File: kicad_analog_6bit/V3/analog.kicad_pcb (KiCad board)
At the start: 2 copper layers, 50 x 23.2 mm, 35 parts, among them P1 Conn_02x06_Odd_Even, P2 Conn_01x04, P3 Conn_01x06, P6 Conn_01x01, P7 Conn_01x01, U1 MAX9108, U2 MAX9108, U3 MAX4610, U4 MAX5259EEE+, U5 MCP1754S-3302xCB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

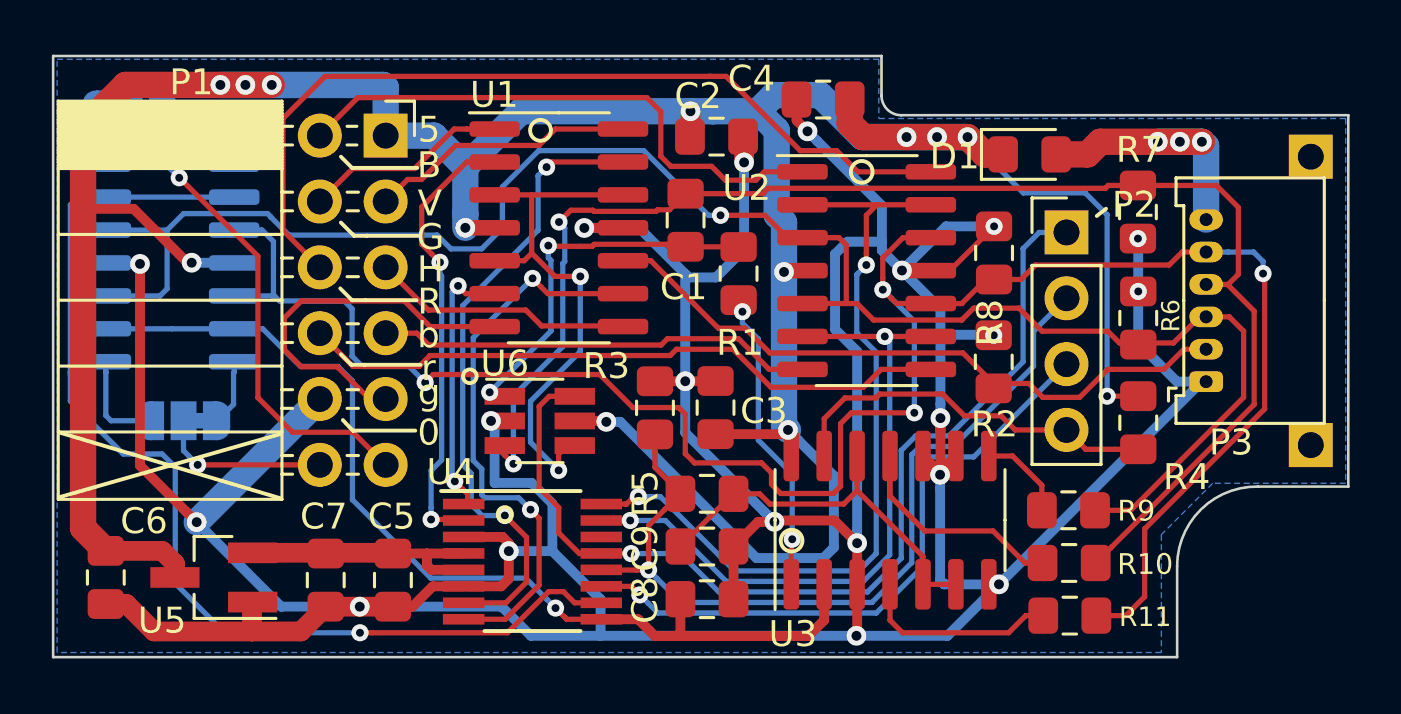
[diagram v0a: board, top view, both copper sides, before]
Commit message: Tweaks to V3 analog PCB
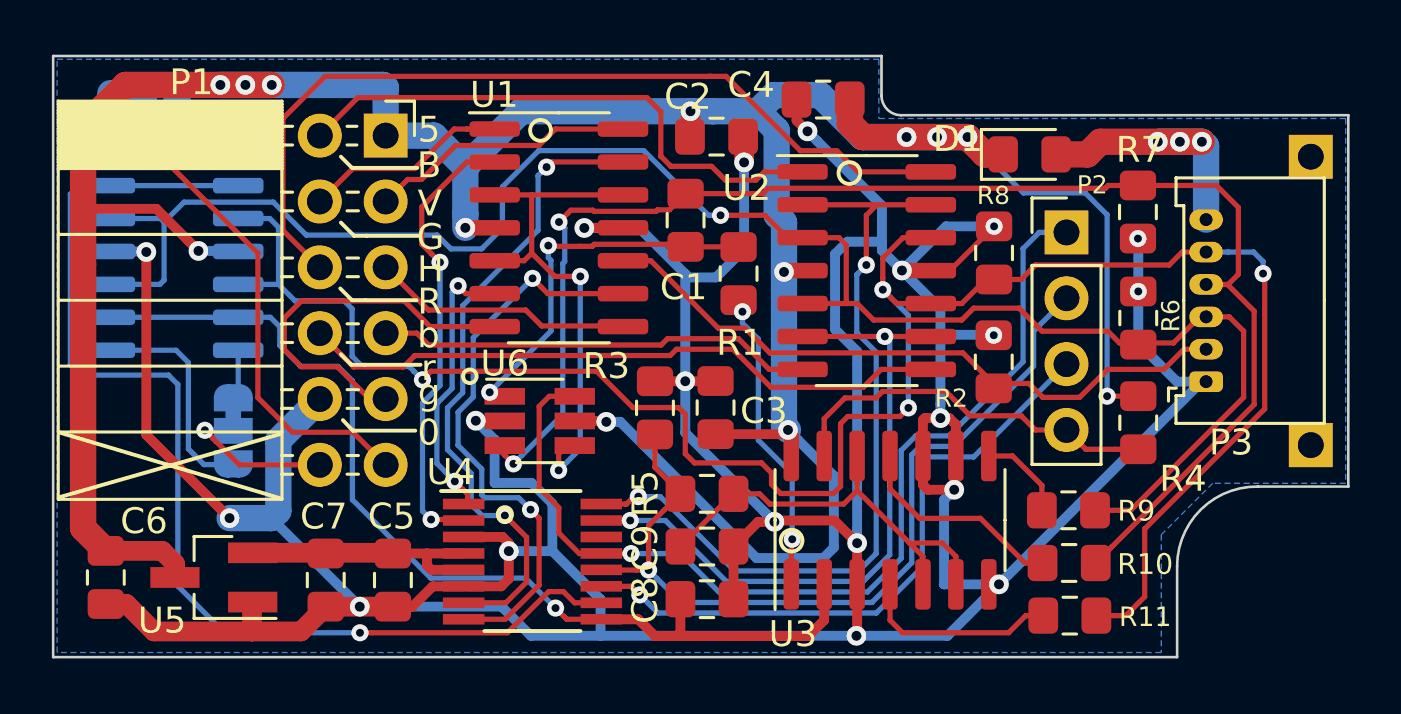
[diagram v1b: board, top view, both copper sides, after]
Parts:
- moved JP2 1.96 mm to (34.5, 45.8), turned to 270 degrees
- moved JP1 0.69 mm to (31.0, 33.0)
- moved U7 0.47 mm to (32.2, 38.8)
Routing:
- net Net-(JP2-Pad3): track 3.85 -> 8.54 mm
- net /GND: track 194.2 -> 197.5 mm
- net /TERM: track 15.3 -> 17.1 mm
- net /SPARE: track 42.2 -> 43.7 mm
- net /SGREEN: track 21.5 -> 20.6 mm
- net Net-(JP1-Pad1): track 2.82 -> 2.06 mm
- net /UV2: track 6.64 -> 7.38 mm
- net Net-(JP1-Pad3): track 3.84 -> 3.18 mm
- net Net-(JP2-Pad1): track 2.55 -> 1.91 mm

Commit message: Updated analog board
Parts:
- R10, R11, R9: value 68R -> 75R
- R6, R7, R8: value 10K -> 47K
- U3: value MAX4610 -> TS12A44514DR
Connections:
- JP1 pad 2: /UV1 -> /UV2
- JP2 pad 2: /UV2 -> /UV1
- P1 pad 11: /UV1 -> /UV2
- P1 pad 12: /UV2 -> /UV1
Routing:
- net /UV2: track 7.38 -> 19.3 mm
- net /UV1: track 19.3 -> 7.38 mm
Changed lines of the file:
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@@
   )
   (setup
-    (last_trace_width 0.381)
+    (last_trace_width 0.2032)
     (user_trace_width 0.2032)
     (user_trace_width 0.381)
@@
       (effects (font (size 1 1) (thickness 0.15)))
     )
-    (fp_text value MAX4610 (at 0 5.28 90) (layer F.Fab)
+    (fp_text value TS12A44514DR (at 0 5.28 90) (layer F.Fab)
       (effects (font (size 1 1) (thickness 0.15)))
     )
@@
       (effects (font (size 0.7 0.7) (thickness 0.11)))
     )
-    (fp_text value 10K (at 0 1.65 90) (layer F.Fab)
+    (fp_text value 47K (at 0 1.65 90) (layer F.Fab)
       (effects (font (size 1 1) (thickness 0.15)))
     )
@@
       (effects (font (size 1 1) (thickness 0.15)))
     )
-    (fp_text value 10K (at 0 1.65 90) (layer F.Fab)
+    (fp_text value 47K (at 0 1.65 90) (layer F.Fab)
       (effects (font (size 1 1) (thickness 0.15)))
     )
@@
       (effects (font (size 0.7 0.7) (thickness 0.12)))
     )
-    (fp_text value 10K (at 0 1.65 90) (layer F.Fab)
+    (fp_text value 47K (at 0 1.65 90) (layer F.Fab)
       (effects (font (size 1 1) (thickness 0.15)))
     )
@@
       (effects (font (size 0.8 0.8) (thickness 0.1)))
     )
-    (fp_text value 68R (at 0 1.65) (layer F.Fab)
+    (fp_text value 75R (at 0 1.65) (layer F.Fab)
       (effects (font (size 1 1) (thickness 0.15)))
     )
@@
       (effects (font (size 0.8 0.8) (thickness 0.1)))
     )
-    (fp_text value 68R (at 0 1.65) (layer F.Fab)
+    (fp_text value 75R (at 0 1.65) (layer F.Fab)
       (effects (font (size 1 1) (thickness 0.15)))
     )
@@
       (effects (font (size 0.75 0.75) (thickness 0.1)))
     )
-    (fp_text value 68R (at 0 1.65) (layer F.Fab)
+    (fp_text value 75R (at 0 1.65) (layer F.Fab)
       (effects (font (size 1 1) (thickness 0.15)))
     )
@@
       (net 1 /GND))
     (pad 11 thru_hole oval (at 0 12.7) (size 1.7 1.7) (drill 1) (layers *.Cu *.Mask)
+      (net 41 /UV2))
+    (pad 12 thru_hole oval (at -2.54 12.7) (size 1.7 1.7) (drill 1) (layers *.Cu *.Mask)
       (net 36 /UV1))
-    (pad 12 thru_hole oval (at -2.54 12.7) (size 1.7 1.7) (drill 1) (layers *.Cu *.Mask)
-      (net 41 /UV2))
     (model ${KISYS3DMOD}/Connector_PinSocket_2.54mm.3dshapes/PinSocket_2x06_P2.54mm_Horizontal.wrl
       (at (xyz 0 0 0))
@@
       ))
     (pad 2 smd rect (at 0 0) (size 1 1.5) (layers B.Cu B.Mask)
-      (net 36 /UV1))
+      (net 41 /UV2))
     (pad 3 smd custom (at 1.3 0) (size 1 0.5) (layers B.Cu B.Mask)
       (net 37 "Net-(JP1-Pad3)") (zone_connect 2)
@@
       ))
     (pad 2 smd rect (at 0 0 270) (size 1 1.5) (layers B.Cu B.Mask)
-      (net 41 /UV2))
+      (net 36 /UV1))
     (pad 1 smd custom (at -1.3 0 270) (size 1 0.5) (layers B.Cu B.Mask)
       (net 39 "Net-(JP2-Pad1)") (zone_connect 2)
@@
   (segment (start 47.862038 46.454062) (end 47.356579 46.959521) (width 0.2032) (layer B.Cu) (net 35))
   (segment (start 47.356579 46.959521) (end 47.02638 47.28972) (width 0.2032) (layer B.Cu) (net 35))
-  (via (at 31.55778 35.04438) (size 0.6604) (drill 0.3048) (layers F.Cu B.Cu) (net 36))
-  (segment (start 35.4262 38.9128) (end 31.887979 35.374579) (width 0.2032) (layer F.Cu) (net 36))
-  (segment (start 31.887979 35.374579) (end 31.55778 35.04438) (width 0.2032) (layer F.Cu) (net 36))
-  (segment (start 35.4262 44.48556) (end 35.4262 38.9128) (width 0.2032) (layer F.Cu) (net 36))
-  (segment (start 36.7597 45.81906) (end 35.4262 44.48556) (width 0.2032) (layer F.Cu) (net 36))
-  (segment (start 39.0965 45.81906) (end 36.7597 45.81906) (width 0.2032) (layer F.Cu) (net 36))
-  (segment (start 40.3538 47.07636) (end 39.0965 45.81906) (width 0.2032) (layer F.Cu) (net 36))
-  (segment (start 31.032 33.93764) (end 31.032 32.98444) (width 0.2032) (layer B.Cu) (net 36))
-  (segment (start 31.032 34.051627) (end 31.032 33.93764) (width 0.2032) (layer B.Cu) (net 36))
-  (segment (start 31.55778 34.577407) (end 31.032 34.051627) (width 0.2032) (layer B.Cu) (net 36))
-  (segment (start 31.55778 35.04438) (end 31.55778 34.577407) (width 0.2032) (layer B.Cu) (net 36))
+  (via (at 33.37896 45.74286) (size 0.6604) (drill 0.3048) (layers F.Cu B.Cu) (net 36))
+  (segment (start 37.8138 47.07636) (end 34.71246 47.07636) (width 0.2032) (layer F.Cu) (net 36))
+  (segment (start 33.709159 46.073059) (end 33.37896 45.74286) (width 0.2032) (layer F.Cu) (net 36))
+  (segment (start 34.71246 47.07636) (end 33.709159 46.073059) (width 0.2032) (layer F.Cu) (net 36))
+  (segment (start 34.62356 45.74286) (end 34.65404 45.77334) (width 0.2032) (layer B.Cu) (net 36))
+  (segment (start 33.37896 45.74286) (end 34.62356 45.74286) (width 0.2032) (layer B.Cu) (net 36))
+  (segment (start 34.45338 45.74286) (end 34.47624 45.76572) (width 0.2032) (layer B.Cu) (net 36))
+  (segment (start 33.37896 45.74286) (end 34.45338 45.74286) (width 0.2032) (layer B.Cu) (net 36))
   (segment (start 32.6165 32.98444) (end 32.332 32.98444) (width 0.2032) (layer B.Cu) (net 37))
   (segment (start 34.66628 35.03422) (end 32.6165 32.98444) (width 0.2032) (layer B.Cu) (net 37))
@@
   (segment (start 32.26644 42.65422) (end 29.71628 42.65422) (width 0.2032) (layer B.Cu) (net 40))
   (segment (start 32.743959 43.131739) (end 32.26644 42.65422) (width 0.2032) (layer B.Cu) (net 40))
-  (via (at 33.37896 45.74286) (size 0.6604) (drill 0.3048) (layers F.Cu B.Cu) (net 41))
-  (segment (start 37.8138 47.07636) (end 34.71246 47.07636) (width 0.2032) (layer F.Cu) (net 41))
-  (segment (start 33.709159 46.073059) (end 33.37896 45.74286) (width 0.2032) (layer F.Cu) (net 41))
-  (segment (start 34.71246 47.07636) (end 33.709159 46.073059) (width 0.2032) (layer F.Cu) (net 41))
-  (segment (start 34.62356 45.74286) (end 34.65404 45.77334) (width 0.2032) (layer B.Cu) (net 41))
-  (segment (start 33.37896 45.74286) (end 34.62356 45.74286) (width 0.2032) (layer B.Cu) (net 41))
-  (segment (start 34.45338 45.74286) (end 34.47624 45.76572) (width 0.2032) (layer B.Cu) (net 41))
-  (segment (start 33.37896 45.74286) (end 34.45338 45.74286) (width 0.2032) (layer B.Cu) (net 41))
+  (via (at 31.55778 35.04438) (size 0.6604) (drill 0.3048) (layers F.Cu B.Cu) (net 41))
+  (segment (start 35.4262 38.9128) (end 31.887979 35.374579) (width 0.2032) (layer F.Cu) (net 41))
+  (segment (start 31.887979 35.374579) (end 31.55778 35.04438) (width 0.2032) (layer F.Cu) (net 41))
+  (segment (start 35.4262 44.48556) (end 35.4262 38.9128) (width 0.2032) (layer F.Cu) (net 41))
+  (segment (start 36.7597 45.81906) (end 35.4262 44.48556) (width 0.2032) (layer F.Cu) (net 41))
+  (segment (start 39.0965 45.81906) (end 36.7597 45.81906) (width 0.2032) (layer F.Cu) (net 41))
+  (segment (start 40.3538 47.07636) (end 39.0965 45.81906) (width 0.2032) (layer F.Cu) (net 41))
+  (segment (start 31.032 33.93764) (end 31.032 32.98444) (width 0.2032) (layer B.Cu) (net 41))
+  (segment (start 31.032 34.051627) (end 31.032 33.93764) (width 0.2032) (layer B.Cu) (net 41))
+  (segment (start 31.55778 34.577407) (end 31.032 34.051627) (width 0.2032) (layer B.Cu) (net 41))
+  (segment (start 31.55778 35.04438) (end 31.55778 34.577407) (width 0.2032) (layer B.Cu) (net 41))
   (segment (start 65.6686 48.82896) (end 65.6686 47.86746) (width 0.2032) (layer F.Cu) (net 42))
   (segment (start 64.5361 46.73496) (end 63.6202 46.73496) (width 0.2032) (layer F.Cu) (net 42))
